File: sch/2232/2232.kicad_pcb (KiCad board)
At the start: 2 copper layers, 80 x 70 mm, 64 parts, among them J1 47346-0001, J2 IDC-06, J3 IDC-06, J4 IDC-10, J5 IDC-10, J6 6P6C, J7 Screw_Terminal_01x06, J8 Screw_Terminal_01x06, U1 FT2232D, U2 AMS1117-3.3, U3 ATmega324A-AU, U4 74LVC244AP, U5 74LVC244AP, U6 ST232BD, Y1 6 MHz, Y2 16 MHz

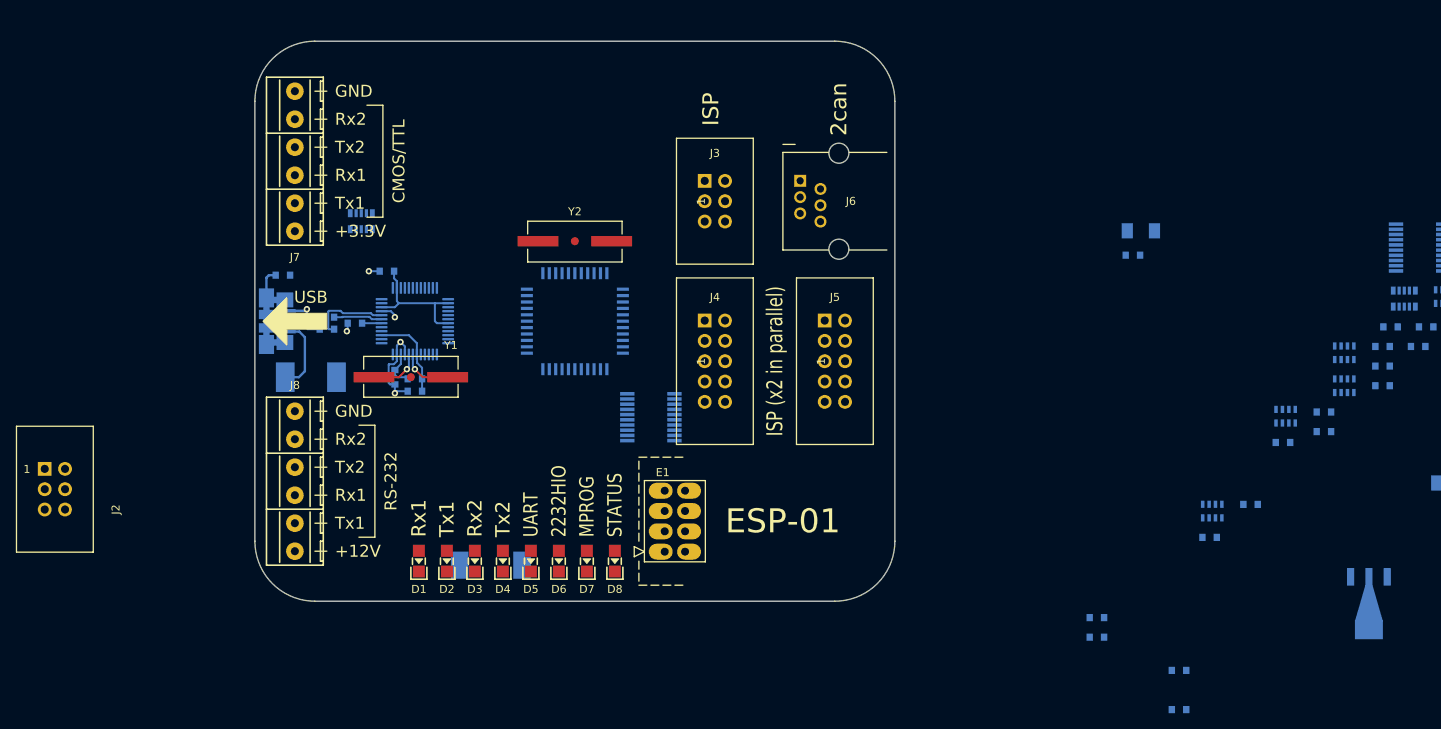
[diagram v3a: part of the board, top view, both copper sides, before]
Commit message: UARTs routed trough connectors
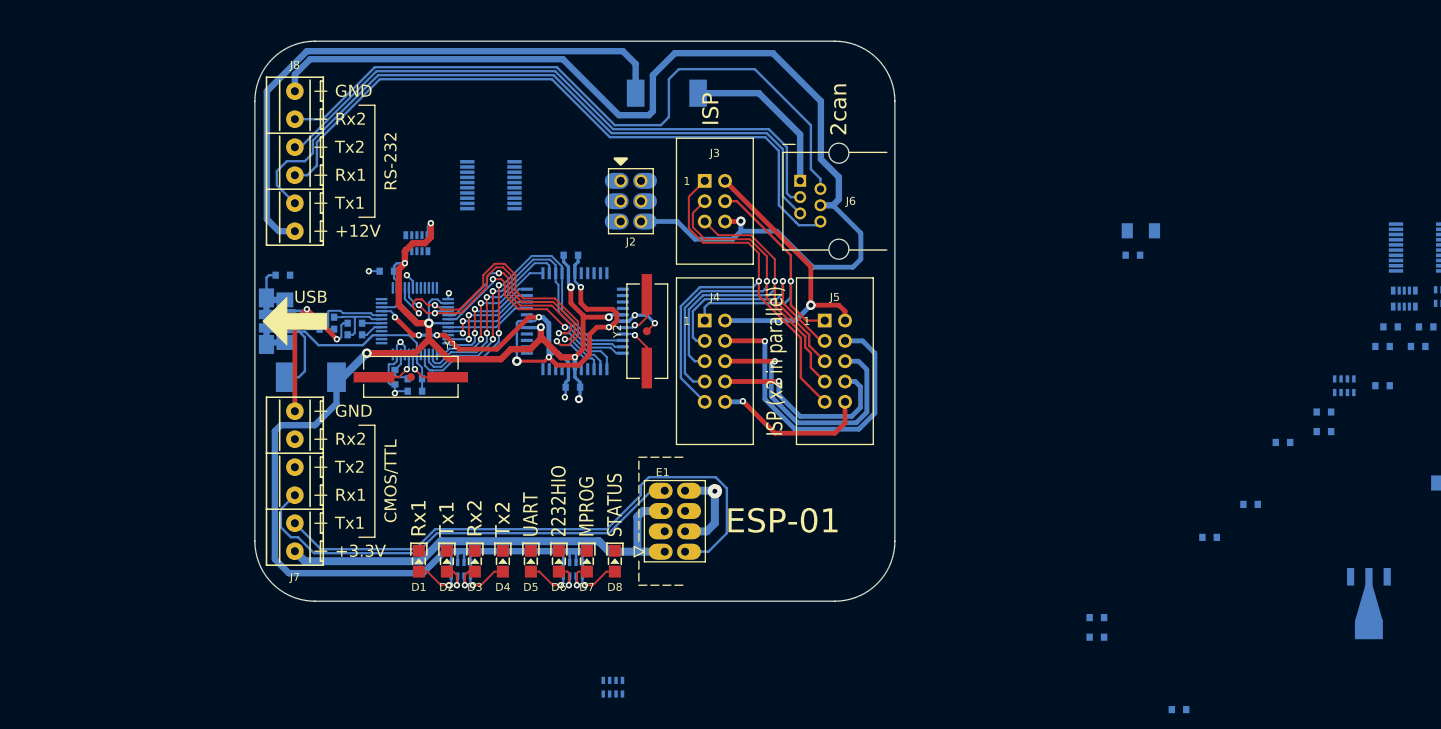
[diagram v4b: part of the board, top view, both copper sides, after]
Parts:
- added C20: 0.22u, NevaDA:C_0603, B.Cu at (99.8, 108.2)
- J2: footprint NevaDA:IDC_Header_Straight_6pins -> NevaDA:PLD-6
- moved RN1 113.7 mm to (85.8, 131.0)
- moved R3 111.2 mm to (72.5, 101.7), turned to 180 degrees
- moved C13 102.4 mm to (99.5, 91.8)
- moved RN2 91.1 mm to (99.8, 131.0)
- moved J2 80.5 mm to (107.0, 85.0), turned to 0 degrees
- moved RN6 78.1 mm to (104.8, 145.8)
- moved D9 63.0 mm to (111.5, 71.5)
- moved J7 40.0 mm to (65.0, 120.0)
- moved J8 40.0 mm to (65.0, 80.0)
- moved U5 35.2 mm to (89.5, 83.0)
- moved Y2 14.4 mm to (109.0, 101.2), turned to 90 degrees
- moved RN3 7.47 mm to (80.2, 90.2)
- turned D1 to 270 degrees
- turned D2 to 270 degrees
- turned D3 to 270 degrees
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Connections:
- R3 pad 2: (no net) -> /USBf_D+
- RN1 pad 5: Net-(D1-Pad2) -> Net-(D4-Pad2)
- RN1 pad 6: Net-(D2-Pad2) -> Net-(D3-Pad2)
- RN1 pad 7: Net-(D3-Pad2) -> Net-(D2-Pad2)
- RN1 pad 8: Net-(D4-Pad2) -> Net-(D1-Pad2)
- RN2 pad 5: Net-(D5-Pad2) -> Net-(D8-Pad2)
- RN2 pad 6: Net-(D6-Pad2) -> Net-(D7-Pad2)
- RN2 pad 7: Net-(D7-Pad2) -> Net-(D6-Pad2)
- RN2 pad 8: Net-(D8-Pad2) -> Net-(D5-Pad2)
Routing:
- net GNDD: track 21.2 -> 296.2 mm, vias 6 -> 21
- net +5V: track 16.8 -> 187.7 mm, vias 0 -> 9
- net /RX2_RSR: track 0.00 -> 87.2 mm
- net /TX1_RSR: track 0.00 -> 86.8 mm
- net /RX1_RSR: track 0.00 -> 84.1 mm
- net /TX2_RSR: track 0.00 -> 77.0 mm
- net Net-(D9-Pad2): track 0.00 -> 72.6 mm
- net /TX1_3VR: track 0.00 -> 72.2 mm
- net /IDC_MISO: track 0.00 -> 63.0 mm, vias 0 -> 1
- net /RX1_3VR: track 0.00 -> 57.3 mm
- net /IDC_CLK: track 0.00 -> 56.4 mm, vias 0 -> 1
- net +3V3: track 0.00 -> 56.4 mm
- net /LED4_~WR: track 0.00 -> 47.7 mm, vias 0 -> 3
- net /IDC_RST: track 0.00 -> 46.9 mm, vias 0 -> 1
- net /PAR_0_T2: track 0.00 -> 44.0 mm, vias 0 -> 2
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
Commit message: All components on-board
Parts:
- moved RN7 138.9 mm to (70.8, 81.8), turned to 270 degrees
- moved C2 129.1 mm to (76.5, 110.2)
- moved U4 125.1 mm to (83.0, 115.8), turned to 180 degrees
- moved C15 121.1 mm to (84.0, 71.8), turned to 90 degrees
- moved RN4 120.9 mm to (85.5, 122.5)
- moved C16 113.9 mm to (95.5, 74.8)
- moved C18 109.1 mm to (95.5, 76.8), turned to 180 degrees
- moved C14 106.6 mm to (94.5, 72.2), turned to 270 degrees
- moved C17 101.8 mm to (96.2, 72.2), turned to 270 degrees
- moved C8 92.7 mm to (117.5, 131.8), turned to 90 degrees
- moved C1 91.6 mm to (80.0, 110.2), turned to 180 degrees
- moved RN5 88.3 mm to (112.8, 79.2), turned to 90 degrees
- moved C10 84.5 mm to (110.0, 101.5)
- moved R6 80.5 mm to (88.8, 114.5), turned to 270 degrees
- moved R7 78.8 mm to (88.8, 118.0), turned to 270 degrees
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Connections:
- RN5 pad 1: /ISP_MOSI -> /ISP_RST
- RN5 pad 2: /ISP_RST -> /ISP_CLK
- RN5 pad 3: /ISP_CLK -> /ISP_MISO
- RN5 pad 4: /ISP_MISO -> /ISP_MOSI
- RN5 pad 5: /IDC_MISO -> /IDC_MOSI
- RN5 pad 6: /IDC_CLK -> /IDC_MISO
- RN5 pad 7: /IDC_RST -> /IDC_CLK
- RN5 pad 8: /IDC_MOSI -> /IDC_RST
- RN6 pad 1: /TX1_3V -> /RX2_3V
- RN6 pad 2: /RX1_3V -> /TX2_3V
- RN6 pad 3: /TX2_3V -> /RX1_3V
- RN6 pad 4: /RX2_3V -> /TX1_3V
- RN6 pad 5: /RX2_3VR -> /TX1_3VR
- RN6 pad 6: /TX2_3VR -> /RX1_3VR
- RN6 pad 7: /RX1_3VR -> /TX2_3VR
- RN6 pad 8: /TX1_3VR -> /RX2_3VR
- U3 pad 21: (no net) -> /EN_UART
- U3 pad 22: (no net) -> /MCU_BUFF
- U3 pad 43: /MCU_BUFF -> (no net)
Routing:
- net GNDD: track 296.2 -> 529.4 mm, vias 21 -> 30
- net +5V: track 187.7 -> 287.6 mm, vias 9 -> 12
- net +3V3: track 56.4 -> 134.9 mm, vias 0 -> 2
- net /LED2: track 0.00 -> 60.3 mm, vias 0 -> 1
- net /LED1: track 0.00 -> 58.6 mm, vias 0 -> 1
- net /USB_reset: track 0.00 -> 49.2 mm, vias 0 -> 3
- net /RX2_RS: track 0.00 -> 26.0 mm, vias 0 -> 2
- net /RX1_3V: track 0.00 -> 25.5 mm, vias 0 -> 2
- net /TX2_RS: track 0.00 -> 25.3 mm, vias 0 -> 2
- net /RX2_3V: track 0.00 -> 21.5 mm
- net /TX1_3V: track 0.00 -> 19.0 mm, vias 0 -> 2
- net /TX1_RS: track 0.00 -> 17.5 mm
- net /RX1_RS: track 0.00 -> 17.3 mm
- net /EEDATA: track 0.00 -> 16.2 mm, vias 0 -> 1
- net /TX2_3V: track 0.00 -> 13.8 mm, vias 0 -> 2
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
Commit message: RN remap
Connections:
- RN3 pad 1: /USB_reset -> /ISP_MISO
- RN3 pad 2: /EEDATA -> /ISP_RST
- RN3 pad 3: /ISP_MISO -> /MCU_BUFF
- RN3 pad 4: /ISP_RST -> /MCU_RST
- RN3 pad 8: /MCU_BUFF -> /USB_reset
- RN3 pad 9: /MCU_RST -> /EEDATA
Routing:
- net GNDD: track 529.4 -> 664.9 mm, vias 30 -> 31
- net /EEDATA: track 16.2 -> 26.7 mm, vias 1 -> 2
- net /USB_reset: track 49.2 -> 59.1 mm, vias 3 -> 4

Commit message: Sides separated
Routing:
- net /RX1_RS_3: track 0.00 -> 50.4 mm, vias 0 -> 1
- net /TX1_RS_3: track 0.00 -> 49.6 mm, vias 0 -> 1
- net /TX2_RS_3: track 0.00 -> 46.6 mm, vias 0 -> 1
- net /RX2_RS_3: track 0.00 -> 45.1 mm, vias 0 -> 1
- net +3V3: track 134.9 -> 175.2 mm
- net /FBUFF: track 0.00 -> 32.7 mm, vias 0 -> 1
- net /FDO_R1: track 0.00 -> 31.5 mm, vias 0 -> 1
- net /FSCK_T1: track 0.00 -> 29.0 mm, vias 0 -> 1
- net /MCU_BUFF: track 0.00 -> 25.7 mm, vias 0 -> 1
- net GNDD: track 664.9 -> 654.1 mm
- net /FDI: track 0.00 -> 6.04 mm
- net /FCS: track 0.00 -> 4.84 mm
- net /EEDATA: track 26.7 -> 25.1 mm
- net /USB_reset: track 59.1 -> 57.8 mm

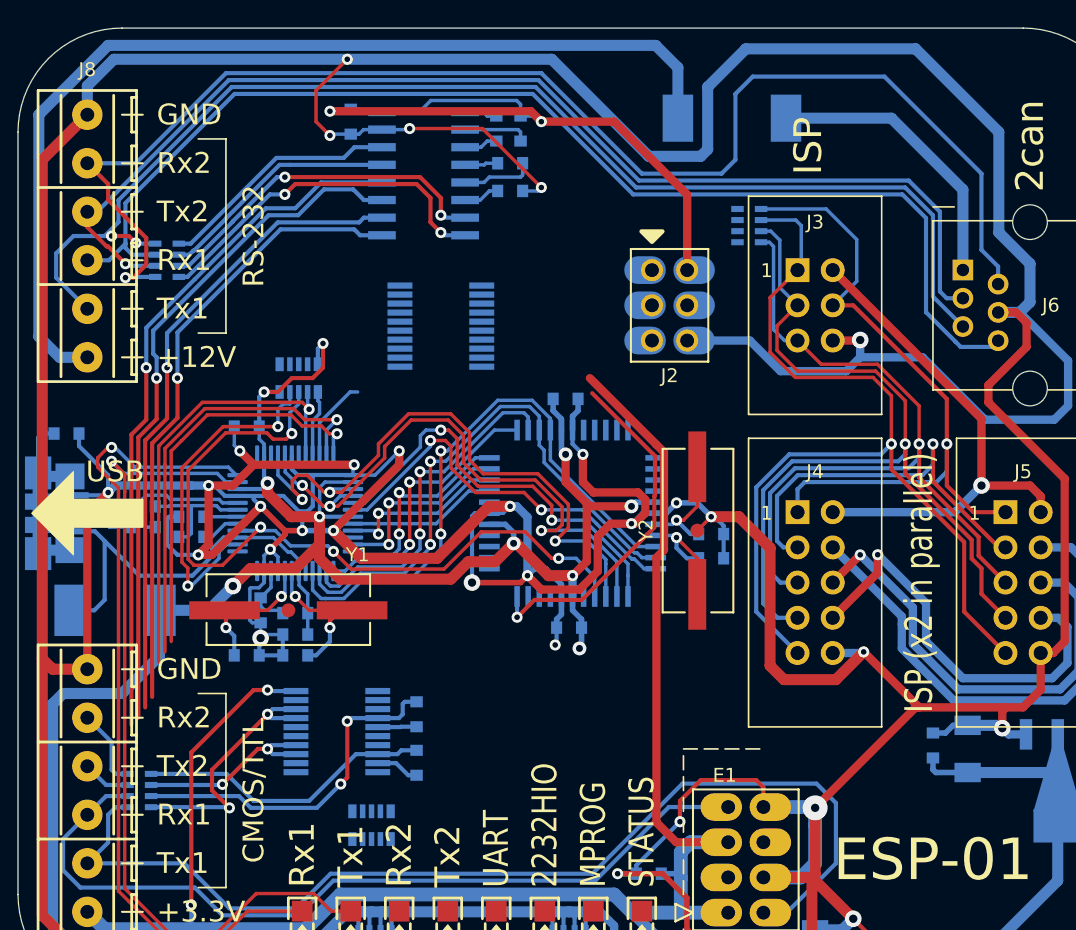
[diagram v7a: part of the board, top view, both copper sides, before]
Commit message: ISP routed
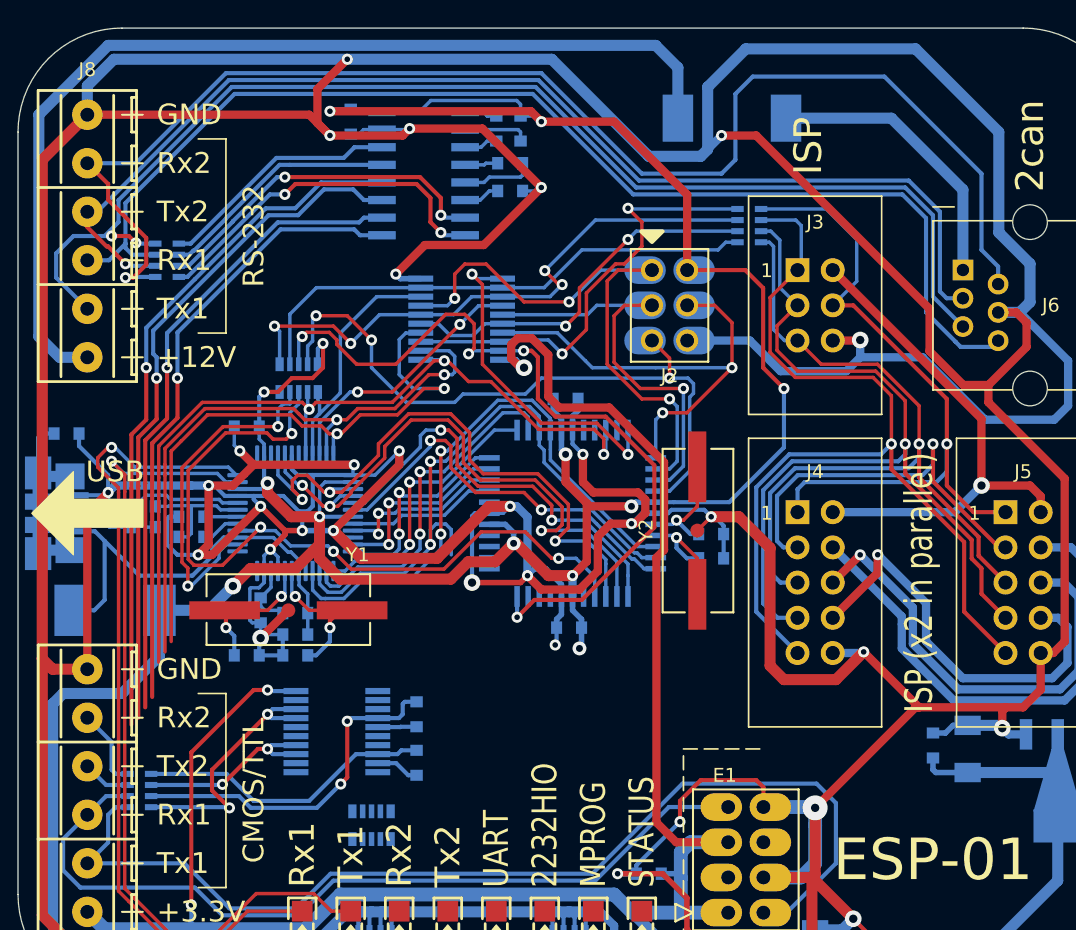
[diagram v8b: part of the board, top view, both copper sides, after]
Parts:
- moved U5 1.58 mm to (92.0, 86.0)
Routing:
- net GNDD: track 654.1 -> 725.4 mm, vias 31 -> 32
- net /MCU_RST: track 0.00 -> 48.3 mm, vias 0 -> 3
- net /ISP_MISO: track 0.00 -> 43.0 mm, vias 0 -> 4
- net /MCU_MISO: track 0.00 -> 42.6 mm, vias 0 -> 3
- net /ISP_RST: track 0.00 -> 38.0 mm
- net /MCU_MOSI: track 0.00 -> 34.4 mm, vias 0 -> 2
- net /ISP_MOSI: track 0.00 -> 32.3 mm, vias 0 -> 2
- net /MCU_BUFF: track 25.7 -> 57.1 mm, vias 1 -> 4
- net /MCU_SCK: track 0.00 -> 31.3 mm, vias 0 -> 1
- net /FBUFF: track 32.7 -> 62.4 mm, vias 1 -> 3
- net +5V: track 287.2 -> 316.2 mm, vias 12 -> 13
- net /ISP_CLK: track 0.00 -> 27.5 mm, vias 0 -> 2
- net /MCU_ROUT: track 0.00 -> 24.1 mm, vias 0 -> 2
- net /FSCK_T1: track 29.0 -> 46.1 mm, vias 1 -> 2
- net /FDO_R1: track 31.5 -> 45.2 mm, vias 1 -> 2
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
